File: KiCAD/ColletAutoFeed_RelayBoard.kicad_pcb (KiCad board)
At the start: 2 copper layers, 139.7 x 111.8 mm, 53 parts, among them J1 1761685-6, J2 2068320202, K1 G5V-1, K2 G5V-1, K3 G5V-1, K4 G5V-1, K5 G5V-1, K6 G5V-1, K7 G5V-1, K8 G5V-1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

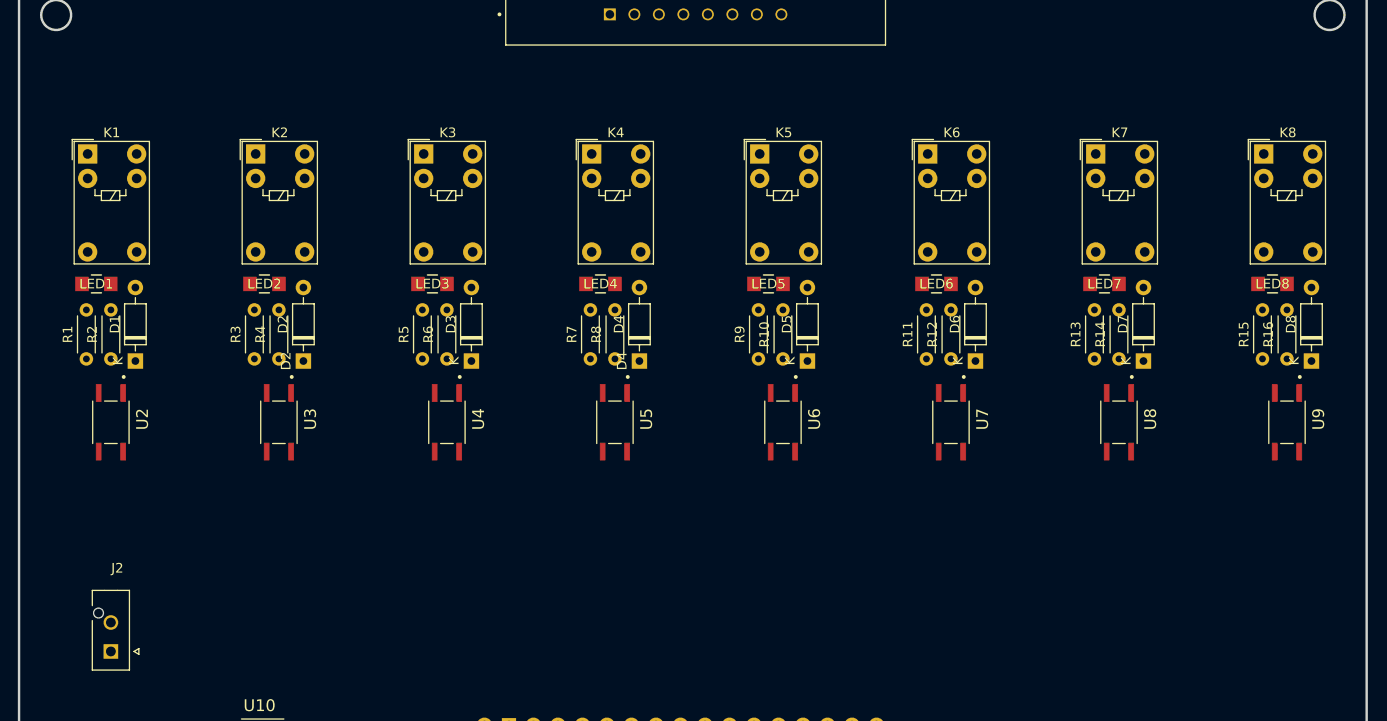
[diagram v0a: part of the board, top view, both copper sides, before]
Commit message: Changed to tht LEDs and added LED to power monitor circuit
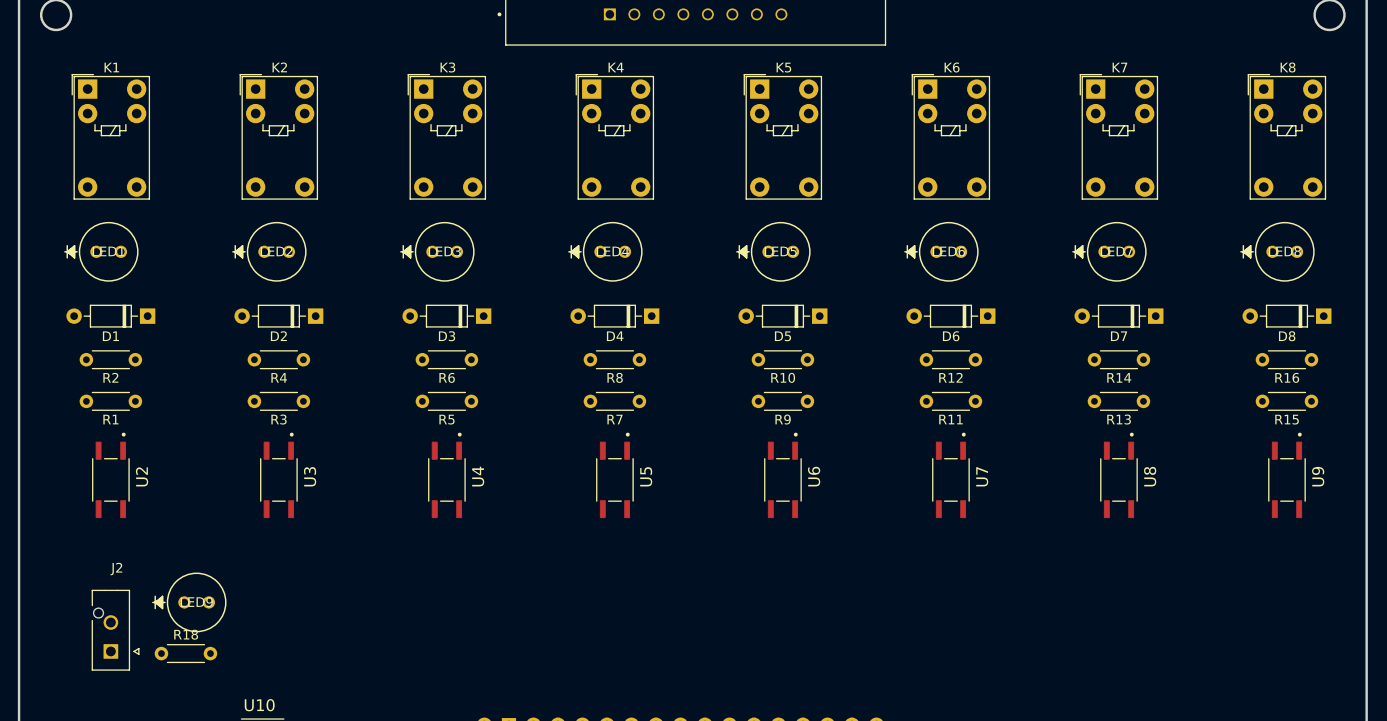
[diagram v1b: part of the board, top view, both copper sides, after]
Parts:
- added LED9: C503B-GCN-CY0C0792, CreeLED Green:C503B_GCN_CY0C0792, F.Cu at (83.8, 106.7)
- added R18: 1.04kΩ, Resistor_THT:R_Axial_DIN0204_L3.6mm_D1.6mm_P5.08mm_Horizontal, F.Cu at (81.4, 112.0)
- LED1, LED2, LED3, LED4, LED5, LED6, LED7, LED8: value 150120BS75000 -> C503B-BCN-CV0Z0461; footprint LED_150120BS75000:LED_150120RS75000_WRE -> CreeLED Blue:C503B_BCN_CV0Z0461
- U10, U2, U3, U4, U5, U6, U7, U8, U9: footprint PC365NJ0000F:SOIC254P700X280-4N -> PC365NJ0000F:PC365NJ0000F
- moved K1 6.72 mm to (73.8, 53.5)
- moved K2 6.72 mm to (91.2, 53.5)
- moved K3 6.72 mm to (108.6, 53.5)
- moved K4 6.72 mm to (126.0, 53.5)
- moved K5 6.72 mm to (143.5, 53.5)
- moved K6 6.72 mm to (160.9, 53.5)
- moved K7 6.72 mm to (178.3, 53.5)
- moved K8 6.72 mm to (195.7, 53.5)
- moved R13 6.72 mm to (183.2, 85.8), turned to 180 degrees
- moved R5 6.72 mm to (113.6, 85.8), turned to 180 degrees
- moved R9 6.72 mm to (148.4, 85.8), turned to 180 degrees
- moved R1 6.72 mm to (78.7, 85.8), turned to 180 degrees
- moved R3 6.72 mm to (96.2, 85.8), turned to 180 degrees
- moved R11 6.72 mm to (165.8, 85.8), turned to 180 degrees
- moved R15 6.72 mm to (200.7, 85.8), turned to 180 degrees
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
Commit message: Started routing
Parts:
- moved D8 22.9 mm to (179.1, 77.1), turned to 0 degrees
- moved K1 20.1 mm to (91.3, 63.4), turned to 180 degrees
- moved D7 18.9 mm to (165.6, 77.1), turned to 0 degrees
- moved J2 18.4 mm to (73.7, 93.5)
- moved U9 15.8 mm to (182.5, 91.4), turned to 180 degrees
- moved R15 15.2 mm to (185.4, 86.1)
- moved R16 15.2 mm to (185.4, 81.7)
- moved K8 15.2 mm to (180.5, 53.5)
- moved D6 14.9 mm to (152.2, 77.1), turned to 0 degrees
- moved LED1 14.8 mm to (89.5, 70.4), turned to 180 degrees
- moved LED8 13.2 mm to (183.5, 70.4), turned to 180 degrees
- moved R1 12.7 mm to (91.4, 86.1)
- moved U2 12.6 mm to (88.6, 91.4), turned to 0 degrees
- moved U8 11.9 mm to (169.1, 91.4), turned to 180 degrees
- moved R13 11.3 mm to (172.0, 86.1)
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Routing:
- net /S1: track 0.00 -> 45.4 mm
- net Net-(D1-A): track 0.00 -> 33.7 mm
- net +24V: track 0.00 -> 26.4 mm
- net Net-(LED1-Pad1): track 0.00 -> 12.7 mm
- net Net-(R1-Pad2): track 0.00 -> 4.45 mm

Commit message: Continued routing
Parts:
- moved R17 19.2 mm to (87.4, 105.7), turned to 90 degrees
- moved U10 18.4 mm to (76.7, 110.2)
- moved K2 11.0 mm to (104.7, 63.4), turned to 180 degrees
- moved K3 11.0 mm to (118.1, 63.4), turned to 180 degrees
- moved K4 11.0 mm to (131.6, 63.4), turned to 180 degrees
- moved K5 11.0 mm to (145.0, 63.4), turned to 180 degrees
- moved K6 11.0 mm to (158.4, 63.4), turned to 180 degrees
- moved K7 11.0 mm to (171.9, 63.4), turned to 180 degrees
- moved K8 11.0 mm to (185.3, 63.4), turned to 180 degrees
- moved U1 10.7 mm to (135.2, 116.3)
- moved LED9 7.95 mm to (76.7, 103.1), turned to 180 degrees
- moved R18 6.59 mm to (83.3, 105.7), turned to 90 degrees
- moved R10 5.08 mm to (140.0, 81.8), turned to 0 degrees
- moved R14 5.08 mm to (166.9, 81.8), turned to 0 degrees
- moved R4 5.08 mm to (99.7, 81.8), turned to 0 degrees
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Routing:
- net +24V: track 26.4 -> 281.2 mm
- net GND: track 0.00 -> 132.6 mm
- net /IO12: track 0.00 -> 77.0 mm
- net /IO1: track 0.00 -> 46.2 mm
- net /S8: track 0.00 -> 43.3 mm
- net /IO16: track 0.00 -> 40.7 mm
- net /IO2: track 0.00 -> 35.4 mm
- net /S2: track 0.00 -> 34.6 mm
- net Net-(D5-A): track 0.00 -> 33.7 mm
- net Net-(D3-A): track 0.00 -> 33.7 mm
- net Net-(D2-A): track 0.00 -> 33.7 mm
- net Net-(D4-A): track 0.00 -> 33.7 mm
- net Net-(D8-A): track 0.00 -> 33.7 mm
- net Net-(D7-A): track 0.00 -> 33.7 mm
- net Net-(D6-A): track 0.00 -> 33.7 mm
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
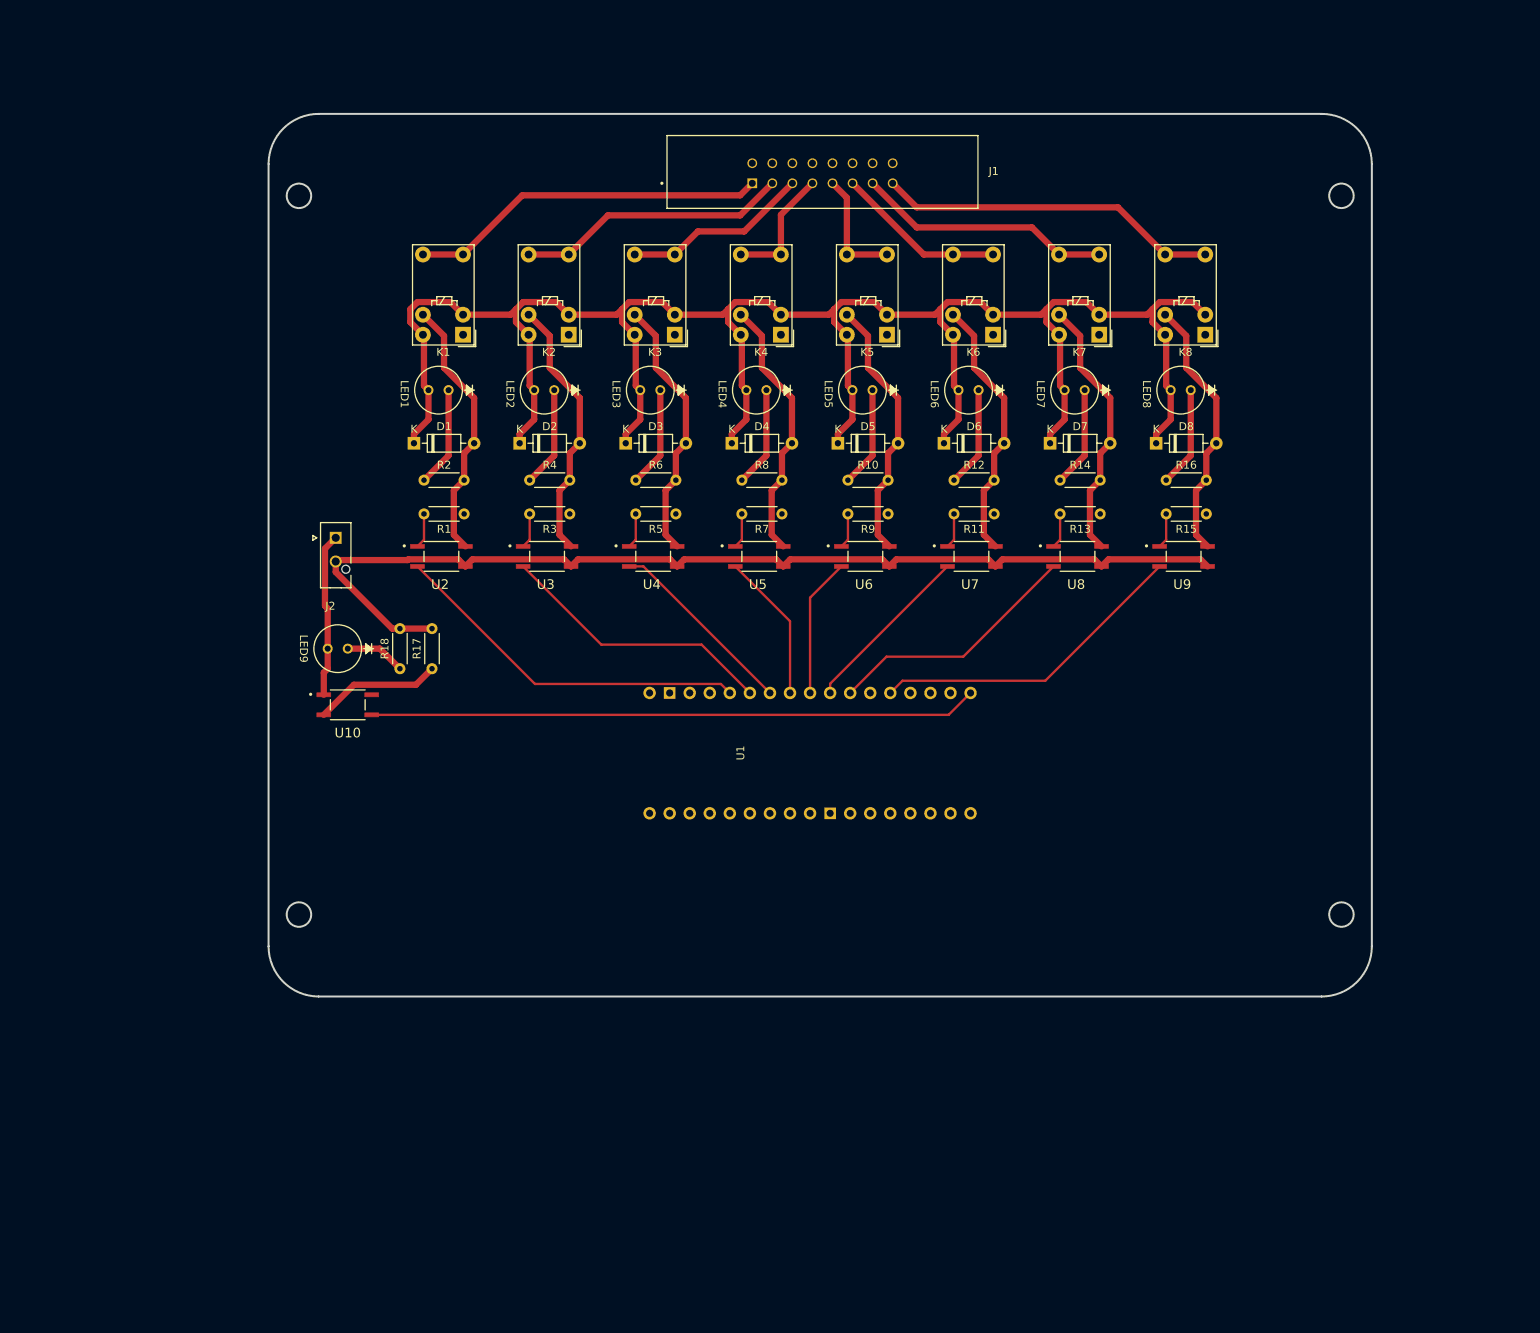
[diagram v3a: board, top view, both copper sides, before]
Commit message: Added ground and power planes
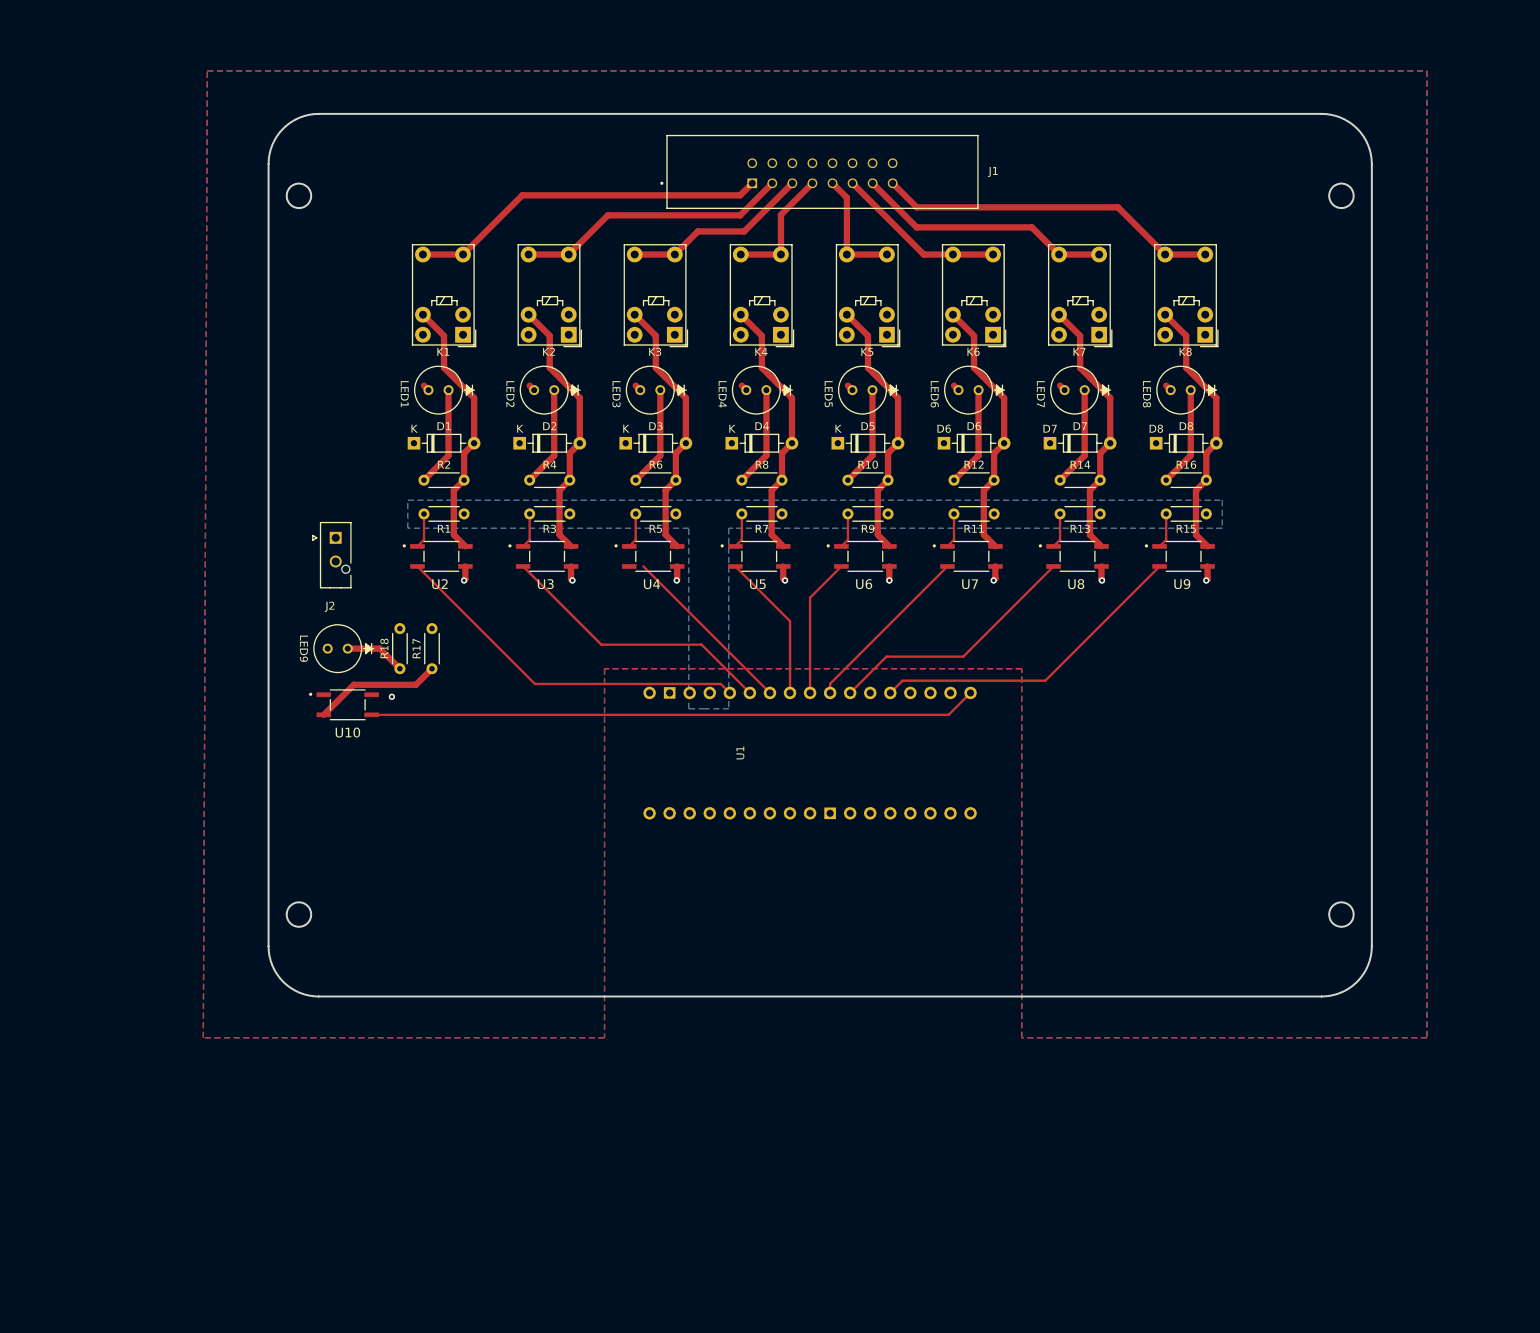
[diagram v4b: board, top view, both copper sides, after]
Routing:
- net +24V: track 281.2 -> 7.96 mm
- net GND: track 132.6 -> 14.9 mm, vias 0 -> 9
- net /IO3: track 24.5 -> 22.7 mm
- added copper zone on F.Cu, net +24V
- added copper zone on B.Cu, net /MCU 3.3v
- added copper zone on B.Cu, net GND

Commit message: Continued working on routing
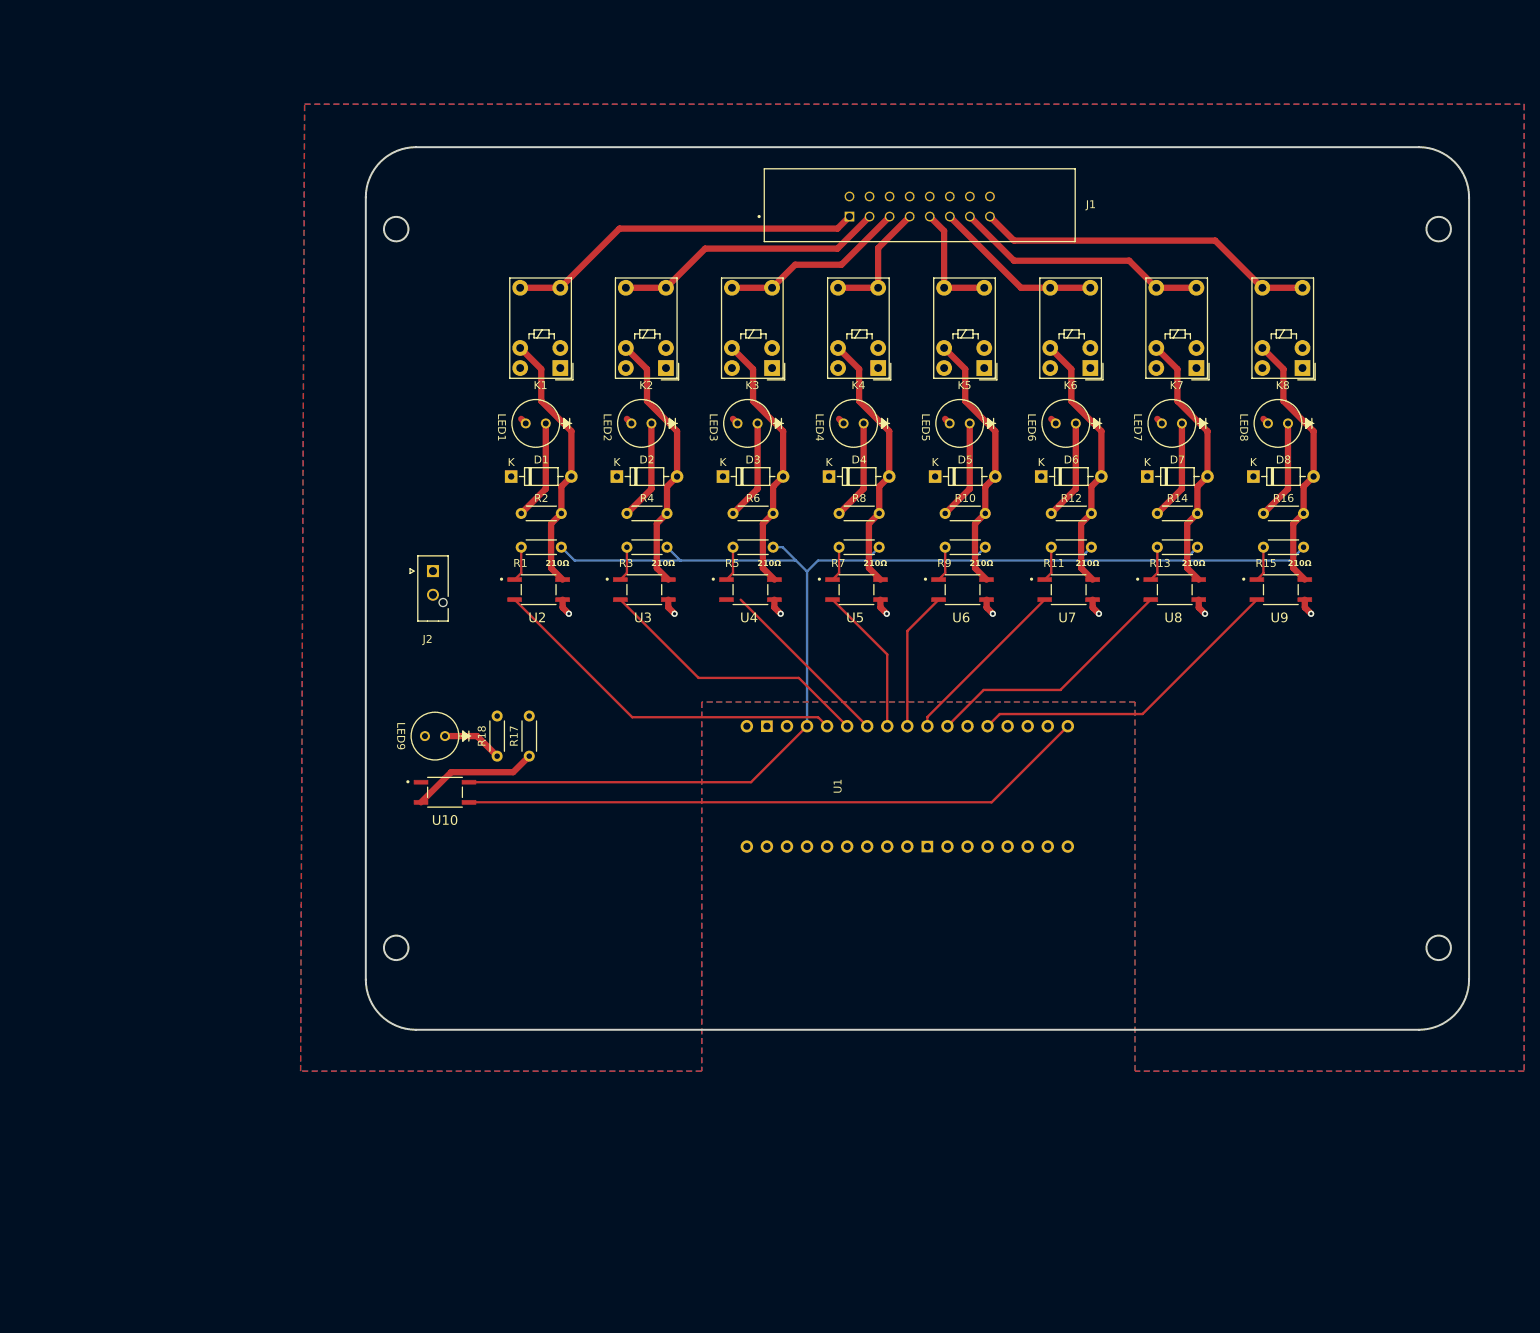
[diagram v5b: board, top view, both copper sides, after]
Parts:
- R1, R11, R13, R15, R3, R5, R7, R9: footprint Resistor_THT:R_Axial_DIN0204_L3.6mm_D1.6mm_P5.08mm_Horizontal -> Resistor:R_Axial_DIN0204_L3.6mm_D1.6mm_P5.08mm_Horizontal-JW
- moved LED9 16.6 mm to (89.0, 114.2)
- moved R18 16.6 mm to (95.6, 116.7)
- moved U10 16.6 mm to (89.0, 121.3)
- moved R17 16.6 mm to (99.7, 116.7)
- moved D7 13.0 mm to (178.0, 81.3)
- moved K4 13.0 mm to (143.9, 67.6)
- moved K7 13.0 mm to (184.2, 67.6)
- moved LED6 13.0 mm to (168.9, 74.6)
- moved R10 13.0 mm to (152.4, 86.0)
- moved R11 13.0 mm to (170.9, 90.3)
- moved R15 13.0 mm to (197.7, 90.3)
- moved U7 13.0 mm to (168.0, 95.7)
- moved U9 13.0 mm to (194.9, 95.7)
- moved D2 13.0 mm to (110.8, 81.3)
- moved D4 13.0 mm to (137.7, 81.3)
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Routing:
- net /MCU 3.3v: track 0.00 -> 177.3 mm
- net /IO12: track 77.0 -> 79.8 mm
- net GND: track 14.9 -> 17.1 mm, vias 9 -> 8
- removed copper zone on B.Cu, net /MCU 3.3v
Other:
- outline, holes or cut-outs redrawn
